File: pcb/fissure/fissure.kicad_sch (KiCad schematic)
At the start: 64 parts, among them J1 Conn_01x04_Female, J2 USB_C_Receptacle_USB2.0, J3 Conn_01x06, J4 Conn_01x06, J5 OLED, J6 Conn_01x06, J7 Conn_01x06, K1 KEY, K10 KEY, K11 KEY, K12 KEY, K13 KEY, K14 KEY, K15 KEY, K16 KEY, K17 KEY, K18 KEY, K19 KEY, K2 KEY, K20 KEY, K3 KEY, K4 KEY, K5 KEY, K6 KEY, K7 KEY, K8 KEY, K9 KEY, Q1 AO3401A, Q2 AO3401A, SW1 SW_Push, SW2 SW_Push, SW3 SW_SPDT, SW4 SW_SPDT, U1 Holyiot_18010, U2 MT25QL128ABA1ESE, U3 LTC4054ES5-4.2, U4 MCP1700-3302E_SOT23

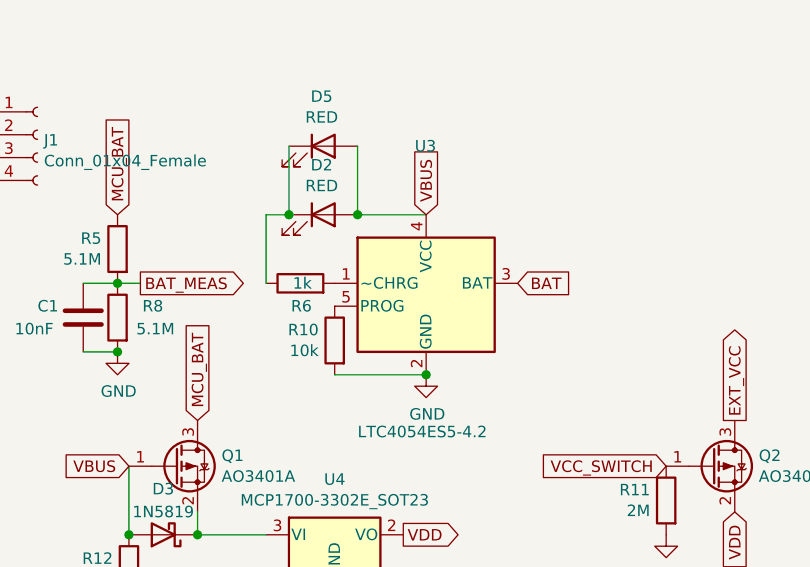
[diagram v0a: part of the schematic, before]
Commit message: stagger update
- middle 2 mm up
- outer index flat with home
- narrower pinky columns
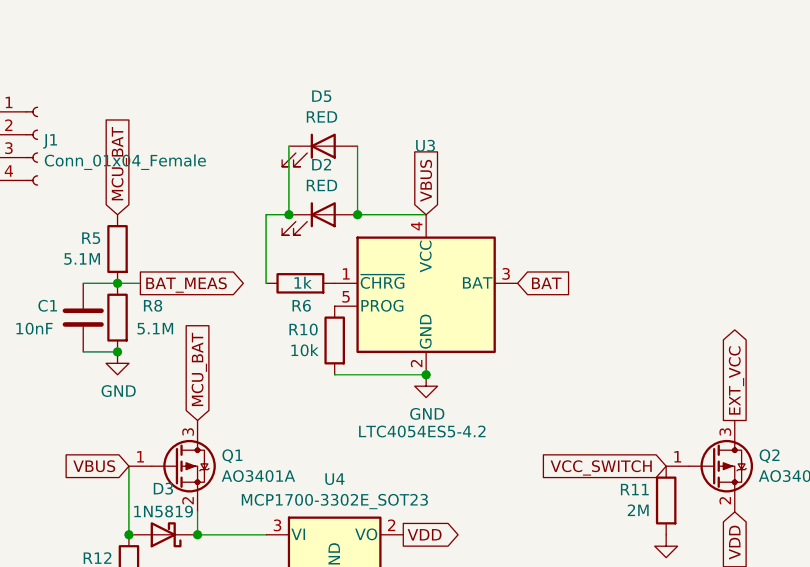
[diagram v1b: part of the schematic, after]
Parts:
- K1, K6: footprint pg1350:PG1350-reversible-no-diode-short -> pg1350:PG1350-reversible-no-diode-short-offcenter-outer
- K16, K17: footprint pg1350:PG1350-reversible-no-diode-short -> pg1350:PG1350-reversible-no-diode-short-offcenter
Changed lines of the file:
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@@
-(kicad_sch (version 20210621) (generator eeschema)
+(kicad_sch (version 20210406) (generator eeschema)
   (paper "A4")
   (junction (at 96.52 110.49) (diameter 1.016) (color 0 0 0 0))
@@
     (property "Reference" "K1" (id 0) (at 219.71 16.51 0))
     (property "Value" "KEY" (id 1) (at 219.71 19.05 0))
-    (property "Footprint" "pg1350:PG1350-reversible-no-diode-short" (id 2) (at 219.71 13.97 0)
+    (property "Footprint" "pg1350:PG1350-reversible-no-diode-short-offcenter-outer" (id 2) (at 219.71 13.97 0)
       (effects (font (size 1.27 1.27)) hide)
     )
@@
     (property "Reference" "K16" (id 0) (at 219.71 43.18 0))
     (property "Value" "KEY" (id 1) (at 219.71 45.72 0))
-    (property "Footprint" "pg1350:PG1350-reversible-no-diode-short" (id 2) (at 219.71 40.64 0)
+    (property "Footprint" "pg1350:PG1350-reversible-no-diode-short-offcenter" (id 2) (at 219.71 40.64 0)
       (effects (font (size 1.27 1.27)) hide)
     )
@@
     (property "Reference" "K17" (id 0) (at 219.71 48.26 0))
     (property "Value" "KEY" (id 1) (at 219.71 50.8 0))
-    (property "Footprint" "pg1350:PG1350-reversible-no-diode-short" (id 2) (at 219.71 45.72 0)
+    (property "Footprint" "pg1350:PG1350-reversible-no-diode-short-offcenter" (id 2) (at 219.71 45.72 0)
       (effects (font (size 1.27 1.27)) hide)
     )
@@
     (property "Reference" "K6" (id 0) (at 241.3 16.51 0))
     (property "Value" "KEY" (id 1) (at 241.3 19.05 0))
-    (property "Footprint" "pg1350:PG1350-reversible-no-diode-short" (id 2) (at 241.3 13.97 0)
+    (property "Footprint" "pg1350:PG1350-reversible-no-diode-short-offcenter-outer" (id 2) (at 241.3 13.97 0)
       (effects (font (size 1.27 1.27)) hide)
     )
@@
     )
     (path "/00000000-0000-0000-0000-0000604b0dbb"
-      (reference "K1") (unit 1) (value "KEY") (footprint "pg1350:PG1350-reversible-no-diode-short")
+      (reference "K1") (unit 1) (value "KEY") (footprint "pg1350:PG1350-reversible-no-diode-short-offcenter-outer")
     )
     (path "/00000000-0000-0000-0000-0000604b388e"
@@
     )
     (path "/00000000-0000-0000-0000-0000604da1bc"
-      (reference "K6") (unit 1) (value "KEY") (footprint "pg1350:PG1350-reversible-no-diode-short")
+      (reference "K6") (unit 1) (value "KEY") (footprint "pg1350:PG1350-reversible-no-diode-short-offcenter-outer")
     )
     (path "/00000000-0000-0000-0000-0000604da1c2"
@@
     )
     (path "/00000000-0000-0000-0000-0000604d8604"
-      (reference "K16") (unit 1) (value "KEY") (footprint "pg1350:PG1350-reversible-no-diode-short")
+      (reference "K16") (unit 1) (value "KEY") (footprint "pg1350:PG1350-reversible-no-diode-short-offcenter")
     )
     (path "/00000000-0000-0000-0000-0000604d860a"
-      (reference "K17") (unit 1) (value "KEY") (footprint "pg1350:PG1350-reversible-no-diode-short")
+      (reference "K17") (unit 1) (value "KEY") (footprint "pg1350:PG1350-reversible-no-diode-short-offcenter")
     )
     (path "/00000000-0000-0000-0000-0000604d8610"

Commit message: Backup
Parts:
- removed J3, J4: Conn_01x06, fissure:bridge-conn, symbol Connector_Generic:Conn_01x06
- removed J6, J7: Conn_01x06, fissure:bridge, symbol Connector_Generic:Conn_01x06
- added J3: Conn_01x0, fissure:bridge-conn, symbol Connector_Generic:Conn_01x05
- added J4: Conn_01x05, fissure:bridge-conn, symbol Connector_Generic:Conn_01x05
- added J6, J7: Conn_01x05, fissure:bridge, symbol Connector_Generic:Conn_01x05
- D1, D2, D4, D5: footprint LED_SMD:LED_1206_3216Metric -> LED_SMD:LED_0805_2012Metric
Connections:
- net BAT: now also J3.2 (Pin_2)
- net BLUE: now also U1.53 (P1.09); no longer U1.36 ([L]_P1.04)
- net GND: now also J3.1 (Pin_1)
- net K1: now also U1.41 ([L]_P1.03); no longer U1.50 (P0.21)
- net K10: now also U1.39 ([L]_P1.02); no longer U1.40 ([L]_P1.01)
- net K11: now also U1.51 (P0.23); no longer U1.53 (P1.09)
- net K12: now also U1.49 (P0.19); no longer U1.51 (P0.23)
- net K18: now also J3.5 (Pin_5)
- net K19: now also J3.4 (Pin_4)
- net K20: now also J3.3 (Pin_3)
- net K5: now also U1.36 ([L]_P1.04); no longer U1.39 ([L]_P1.02)
- net K6: now also U1.50 (P0.21); no longer U1.52 (P0.12)
- net K9: now also U1.40 ([L]_P1.01); no longer U1.41 ([L]_P1.03)
- net RGB: now also U1.52 (P0.12); no longer U1.49 (P0.19)
- net bridge_BAT: now also J6.2 (Pin_2), J7.2 (Pin_2)
- net bridge_GND: now also J6.1 (Pin_1), J7.1 (Pin_1)
- net thumb_BAT: now also J4.2 (Pin_2)
- net thumb_GND: now also J4.1 (Pin_1)
- net thumb_K18: now also J4.5 (Pin_5)
- net thumb_K19: now also J4.4 (Pin_4)
- net thumb_K20: now also J4.3 (Pin_3)
- new net: J6.3 (Pin_3), J7.3 (Pin_3)
- new net: J6.4 (Pin_4), J7.4 (Pin_4)
- new net: J6.5 (Pin_5), J7.5 (Pin_5)
